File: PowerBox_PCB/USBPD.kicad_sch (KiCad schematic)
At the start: 8 parts

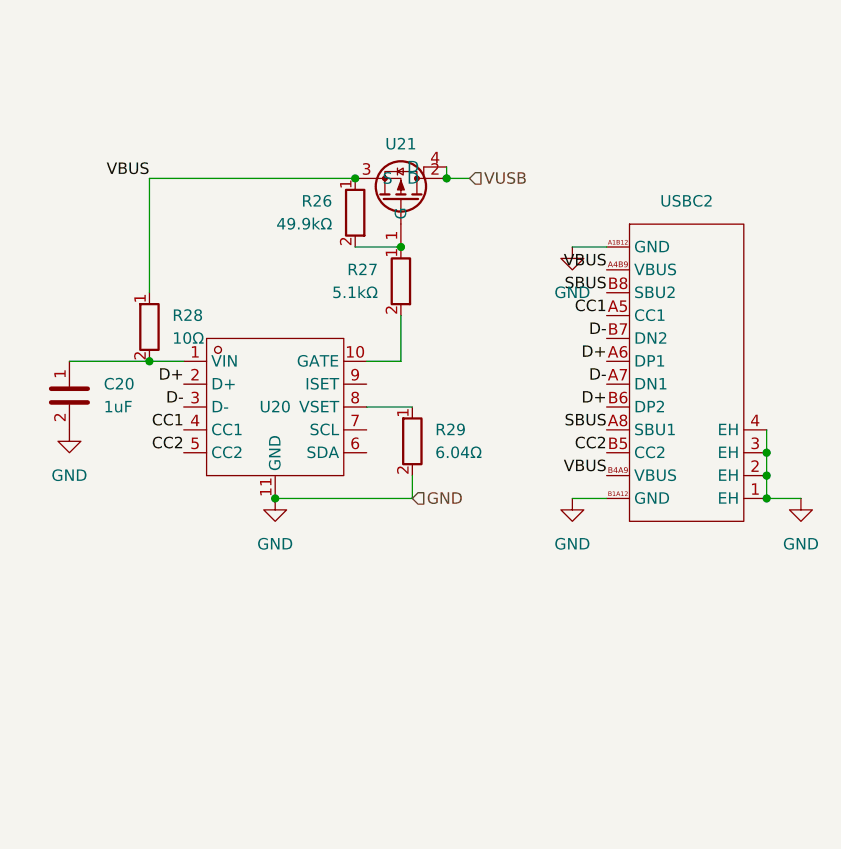
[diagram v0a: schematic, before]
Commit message: add indicator lights
add indicator lights
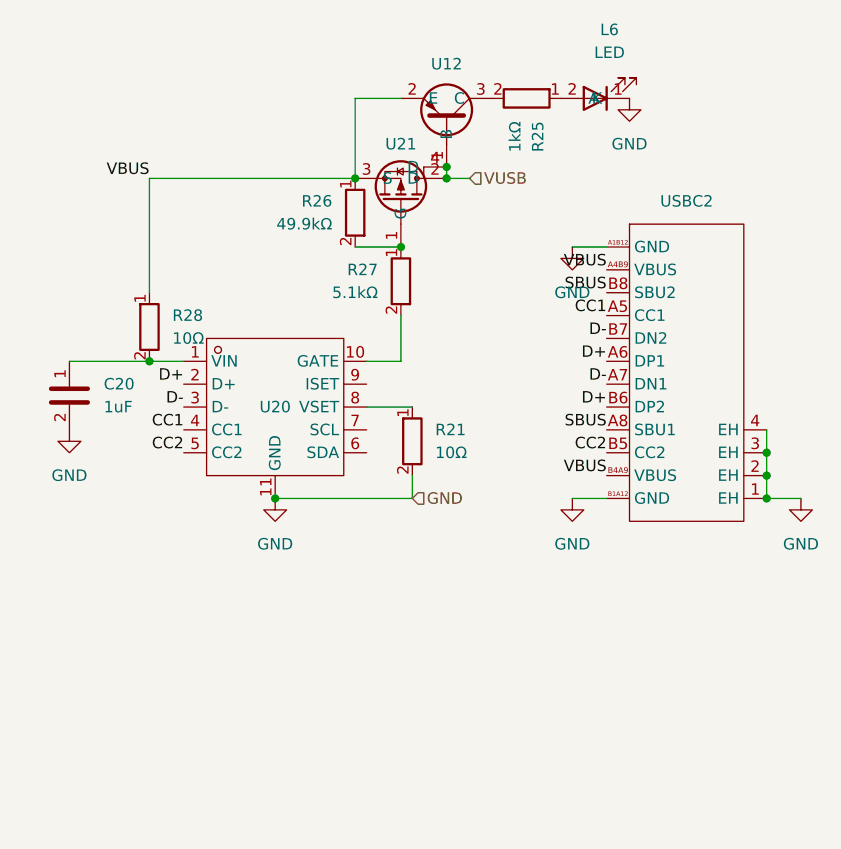
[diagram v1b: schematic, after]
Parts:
- removed R29: 6.04Ω, Resistor_SMD:R_0805_2012Metric_Pad1.20x1.40mm_HandSolder, symbol Custom_Symbols:6.04Res
- added L6: LED, LED_SMD:LED_0805_2012Metric_Pad1.15x1.40mm_HandSolder, symbol Custom_Symbols:LED
- added R21: 10Ω, Resistor_SMD:R_0805_2012Metric_Pad1.20x1.40mm_HandSolder, symbol Custom_Symbols:10Res
- added R25: 1kΩ, Resistor_SMD:R_0805_2012Metric_Pad1.20x1.40mm_HandSolder, symbol Custom_Symbols:1kRes
- added U12: (no value), Package_TO_SOT_SMD:SOT-23, symbol Ideal_Diode:PNP
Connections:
- net GND: now also L6.1 (K), R21.2
- net VBUS: now also U12.2 (E)
- net VUSB: now also U12.1 (B)
- net at U20.8 (VSET): now also R21.1
- new net: R25.2, U12.3 (C)
- new net: L6.2 (A), R25.1

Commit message: .
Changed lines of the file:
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@@
 	(wire
 		(pts
-			(xy 157.48 74.93) (xy 161.29 74.93)
+			(xy 152.4 74.93) (xy 161.29 74.93)
 		)
 		(stroke
@@
 	(wire
 		(pts
-			(xy 157.48 102.87) (xy 161.29 102.87)
+			(xy 152.4 102.87) (xy 161.29 102.87)
 		)
 		(stroke
@@
 	(symbol
 		(lib_id "power:GND")
-		(at 157.48 102.87 0)
+		(at 152.4 102.87 0)
 		(unit 1)
 		(body_style 1)
@@
 		(fields_autoplaced yes)
 		(property "Reference" "#PWR029"
-			(at 157.48 109.22 0)
+			(at 152.4 109.22 0)
 			(hide yes)
 			(show_name no)
@@
 		)
 		(property "Value" "GND"
-			(at 157.48 107.95 0)
+			(at 152.4 107.95 0)
 			(show_name no)
 			(do_not_autoplace no)
@@
 		)
 		(property "Footprint" ""
-			(at 157.48 102.87 0)
+			(at 152.4 102.87 0)
 			(hide yes)
 			(show_name no)
@@
 		)
 		(property "Datasheet" ""
-			(at 157.48 102.87 0)
+			(at 152.4 102.87 0)
 			(hide yes)
 			(show_name no)
@@
 		)
 		(property "Description" "Power symbol creates a global label with name \"GND\" , ground"
-			(at 157.48 102.87 0)
+			(at 152.4 102.87 0)
 			(hide yes)
 			(show_name no)
@@
 		(lib_id "Custom_Symbols:10Res")
 		(at 110.49 83.82 0)
+		(mirror y)
 		(unit 1)
 		(body_style 1)
@@
 		(in_pos_files yes)
 		(dnp no)
-		(fields_autoplaced yes)
 		(property "Reference" "R28"
-			(at 113.03 82.5499 0)
+			(at 107.95 82.5499 0)
 			(show_name no)
 			(do_not_autoplace no)
@@
 		)
 		(property "Value" "10Ω"
-			(at 113.03 85.0899 0)
+			(at 107.95 85.0899 0)
 			(show_name no)
 			(do_not_autoplace no)
@@
 	(symbol
 		(lib_id "power:GND")
-		(at 157.48 74.93 0)
+		(at 152.4 74.93 0)
 		(unit 1)
 		(body_style 1)
@@
 		(fields_autoplaced yes)
 		(property "Reference" "#PWR016"
-			(at 157.48 81.28 0)
+			(at 152.4 81.28 0)
 			(hide yes)
 			(show_name no)
@@
 		)
 		(property "Value" "GND"
-			(at 157.48 80.01 0)
+			(at 152.4 80.01 0)
 			(show_name no)
 			(do_not_autoplace no)
@@
 		)
 		(property "Footprint" ""
-			(at 157.48 74.93 0)
+			(at 152.4 74.93 0)
 			(hide yes)
 			(show_name no)
@@
 		)
 		(property "Datasheet" ""
-			(at 157.48 74.93 0)
+			(at 152.4 74.93 0)
 			(hide yes)
 			(show_name no)
@@
 		)
 		(property "Description" "Power symbol creates a global label with name \"GND\" , ground"
-			(at 157.48 74.93 0)
-			(hide yes)
-			(show_name no)
+			(at 152.4 74.93 0)
+			(hide yes)
+			(show_name no)

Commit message: fix bom
bom
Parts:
- U12: value (none) -> MMBT3906LT1G
- U20: value (none) -> HUSB238_002DD
- U21: value (none) -> DMP6023LE-13
- USBC2: value (none) -> USBC_Port
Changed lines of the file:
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@@
 			)
 		)
-		(property "Value" ""
-			(at 143.51 58.42 0)
+		(property "Value" "MMBT3906LT1G"
+			(at 143.51 52.578 90)
 			(show_name no)
 			(do_not_autoplace no)
@@
 			)
 		)
-		(property "Value" ""
-			(at 138.43 67.31 0)
+		(property "Value" "DMP6023LE-13"
+			(at 148.844 71.12 90)
 			(show_name no)
 			(do_not_autoplace no)
@@
 		(in_pos_files yes)
 		(dnp no)
-		(fields_autoplaced yes)
 		(property "Reference" "USBC2"
 			(at 170.18 69.85 0)
@@
 			)
 		)
-		(property "Value" ""
-			(at 170.18 88.9 0)
+		(property "Value" "USBC_Port"
+			(at 170.18 107.188 0)
 			(show_name no)
 			(do_not_autoplace no)
@@
 			)
 		)
-		(property "Value" ""
-			(at 124.46 92.71 0)
-			(show_name no)
-			(do_not_autoplace no)
+		(property "Value" "HUSB238_002DD"
+			(at 124.46 83.82 0)
+			(show_name no)
+			(do_not_autoplace no)

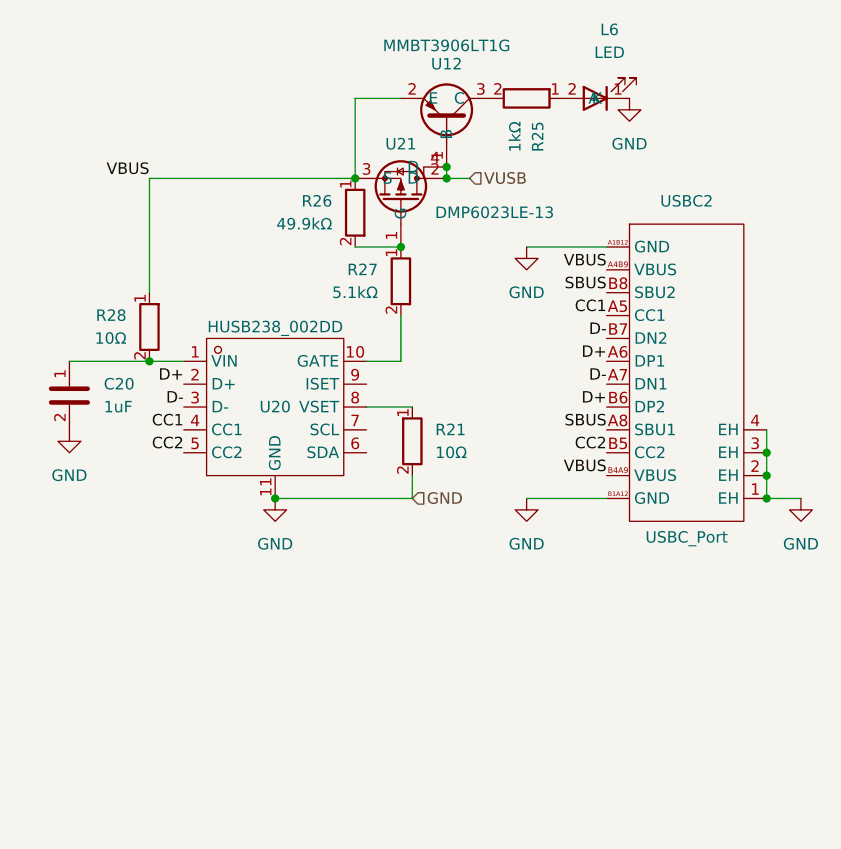
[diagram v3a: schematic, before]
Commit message: Changed HUSB238 to CH221K
HUSB238 Went out of stock so changed to CH221K
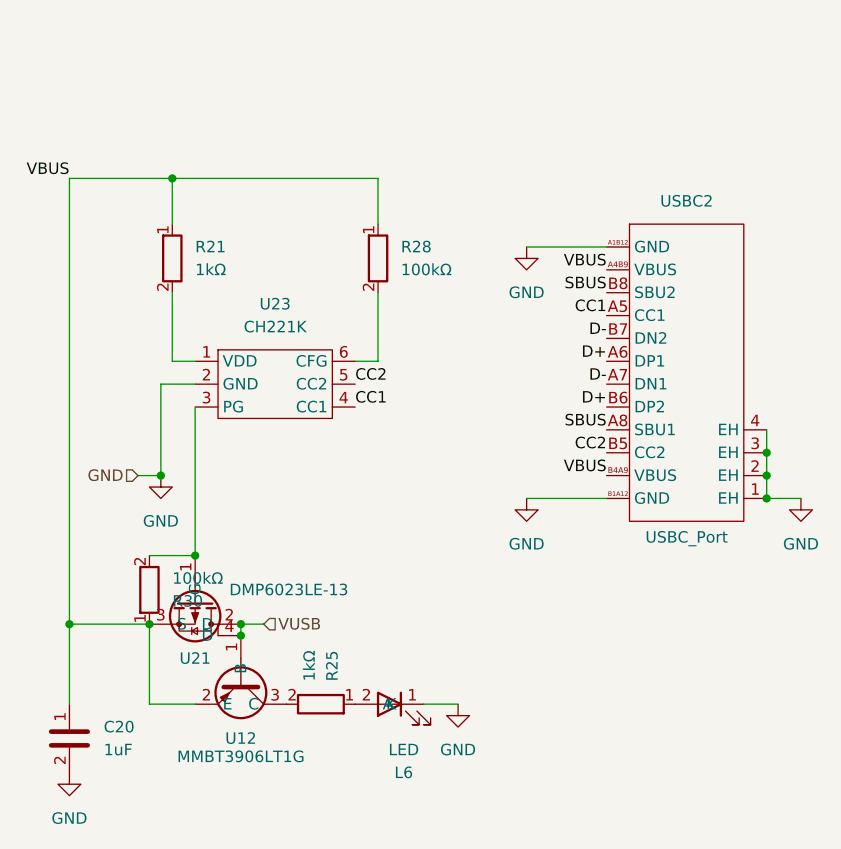
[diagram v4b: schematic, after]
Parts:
- removed R21, R28: 10Ω, Resistor_SMD:R_0805_2012Metric_Pad1.20x1.40mm_HandSolder, symbol Custom_Symbols:10Res
- removed R26: 49.9kΩ, Resistor_SMD:R_0805_2012Metric_Pad1.20x1.40mm_HandSolder, symbol Custom_Symbols:49.9kRes
- removed R27: 5.1kΩ, Resistor_SMD:R_0805_2012Metric_Pad1.20x1.40mm_HandSolder, symbol Custom_Symbols:5.1kRes
- removed U20: HUSB238_002DD, Custom_Footprints:DFN-10_L3.0-W3.0-P0.50-BL-EP2.5, symbol USBPD:HUSB238_002DD
- added R21: 1kΩ, Resistor_SMD:R_0805_2012Metric_Pad1.20x1.40mm_HandSolder, symbol Custom_Symbols:1kRes
- added R28, R30: 100kΩ, Resistor_SMD:R_0805_2012Metric_Pad1.20x1.40mm_HandSolder, symbol USBPD:100kRes
- added U23: CH221K, Package_TO_SOT_SMD:SOT-23-6, symbol USBPD:CH221K
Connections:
- net CC1: now also U23.4 (CC1)
- net CC2: now also U23.5 (CC2)
- net GND: now also U23.2 (GND)
- net VBUS: now also C20.1, R21.1, R28.1, R30.1
- net at U21.1 (G): now also R30.2, U23.3 (PG)
- new net: R28.2, U23.6 (CFG)
- new net: R21.2, U23.1 (VDD)
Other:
- moved on the sheet: C20
